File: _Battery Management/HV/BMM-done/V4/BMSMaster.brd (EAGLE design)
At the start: 83.8 x 91.4 mm, 129 parts, among them J1 M2S02B-PASK-2(LF)(SN), J10 IMD, J14 USB_B_RA, J2 M2S02B-PASK-2(LF)(SN), J3 M8S08B-PASK-2(LF)(SN), J5 M16_M_194280016, J6 M2770166, J7 M2770166, J8 M2770166, J9 M2770166, K1 ADJ14024, Q1 IRFR9120TRPBF, Q3 BSS123, U1 SN75HVD08DRMSOP, U10 NC7S14M5X, U11 LTC6820, U12 FT24C64A, U17 TPS542951PWPR, U23 NUD3160DMT1G, U3 FT230X, U4 SN74LVC2G241, U5 NC7S14M5X, U6 DSPIC33FJ128GP804, U7 DMG6602SVTQ, U8 LTC6820, U9 MAX823TEUK+T_3.08, Y1 12Mhz

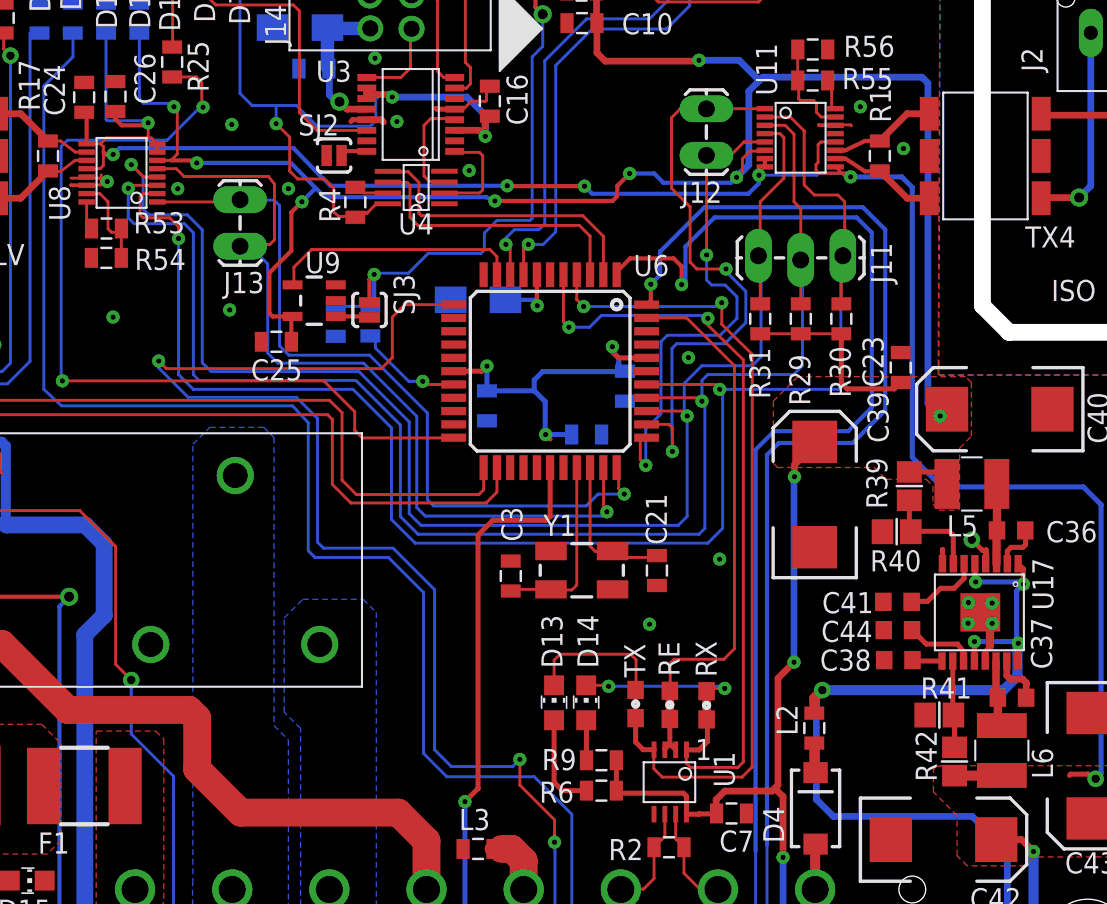
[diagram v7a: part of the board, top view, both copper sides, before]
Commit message: 
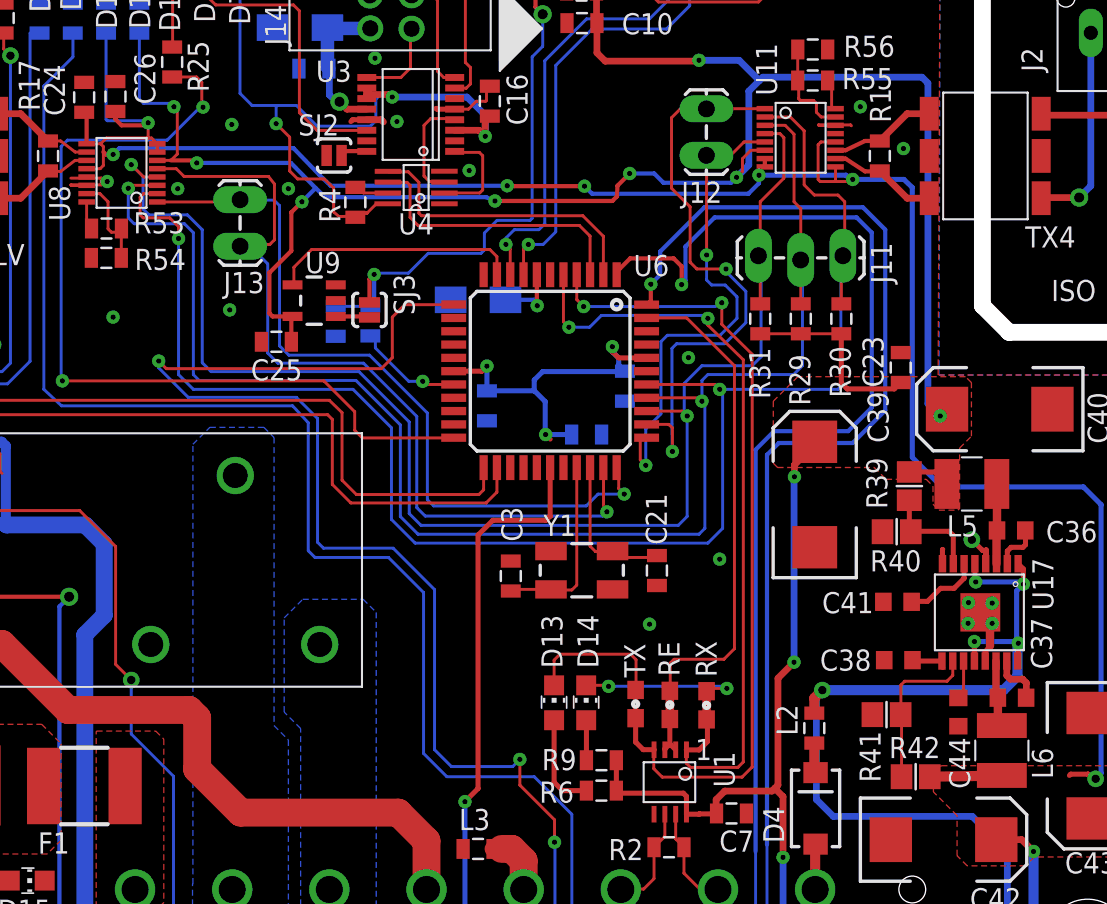
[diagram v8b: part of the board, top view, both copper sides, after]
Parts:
- moved C44 6.12 mm to (71.2, 42.5), turned to 270 degrees
- moved R41 3.18 mm to (66.9, 42.4)
- moved R42 2.51 mm to (68.7, 38.6), turned to 0 degrees
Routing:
- net N$103: track 5.23 -> 10.9 mm
- net +5V: track 220.6 -> 222.8 mm
- net N$77: track 4.23 -> 2.35 mm
